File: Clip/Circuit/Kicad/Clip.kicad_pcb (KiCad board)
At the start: 2 copper layers, 13.5 x 21.8 mm, 3 parts, among them J1 Conn_01x05_Male, J2 Conn_01x05_Male

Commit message: 更新电路板
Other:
- outline, holes or cut-outs redrawn
- board text added: "Ver.1.2"
- board text removed: "Ver.1.1"

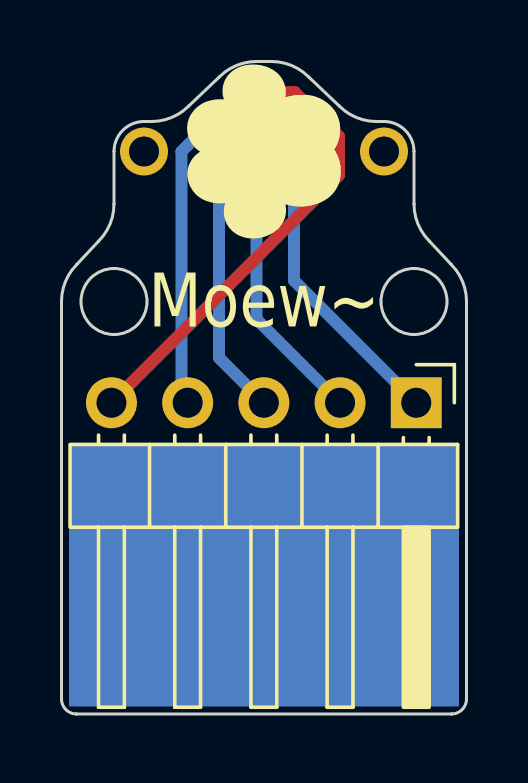
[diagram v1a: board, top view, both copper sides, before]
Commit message: 尺寸凑整 优化走线
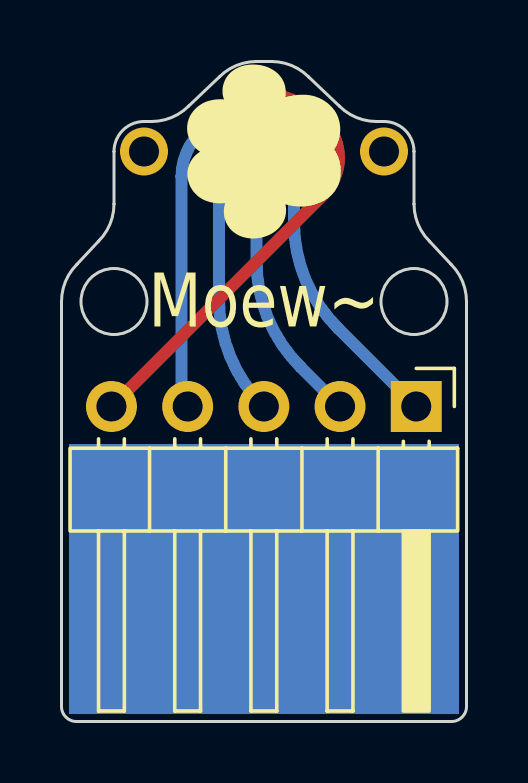
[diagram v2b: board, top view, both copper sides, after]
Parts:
- moved J1 0.12 mm to (172.1, 107.8)
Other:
- board size 13.5 x 21.8 mm -> 13.5 x 22 mm
